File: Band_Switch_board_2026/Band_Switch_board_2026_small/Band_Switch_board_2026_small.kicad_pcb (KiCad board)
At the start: 2 copper layers, 90 x 40 mm, 29 parts, among them J1 KMDGX-8S-N, J2 AUX Out, J3 PTT Rig, J4 ICOM Band, J5 I2C Bus, J6 AUX Out, J7 PTT, J8 ADC Module, U1 ADS1015IDGS

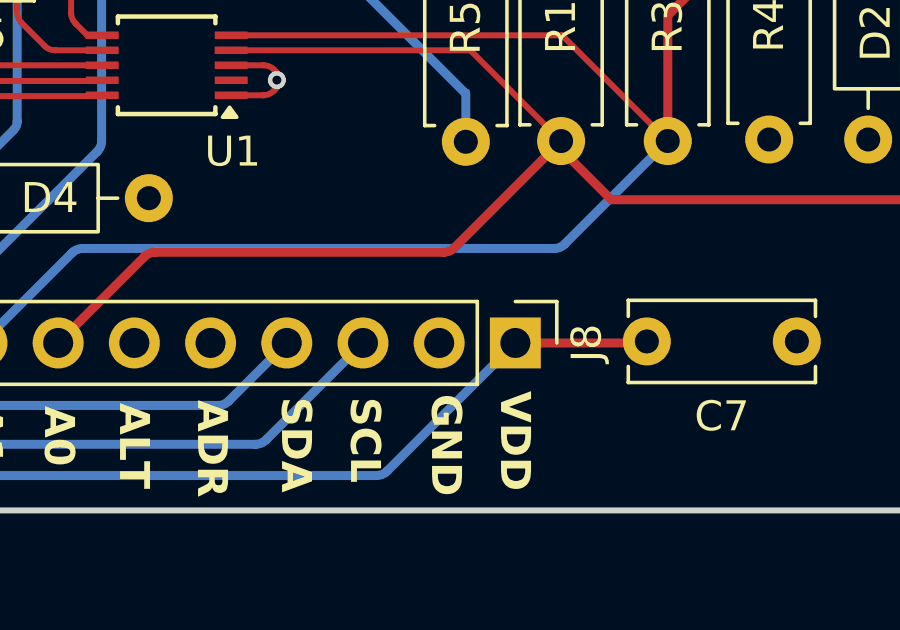
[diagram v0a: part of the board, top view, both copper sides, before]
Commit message: update pcb files to kicad 10
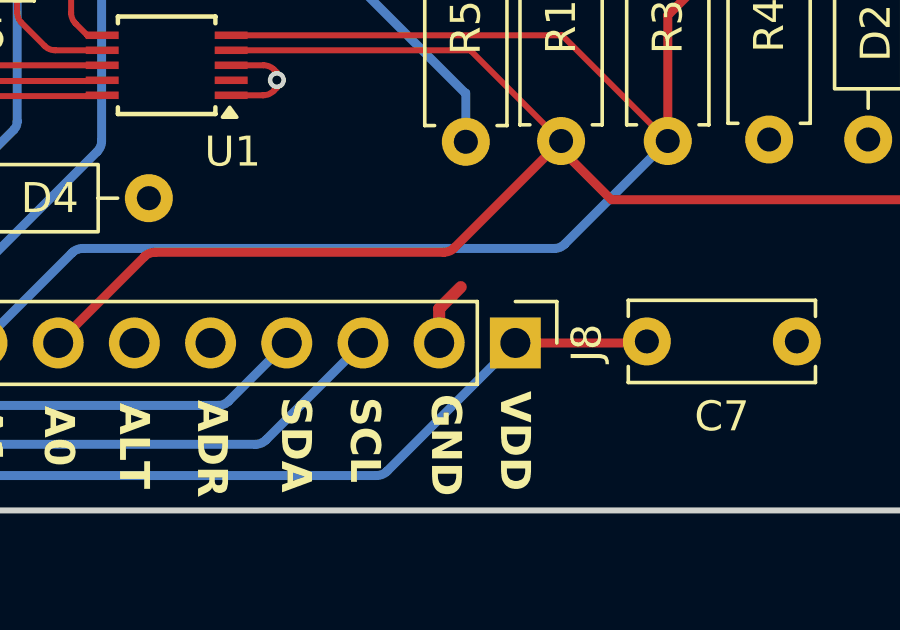
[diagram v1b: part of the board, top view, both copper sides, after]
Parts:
- J8: value ADC Module -> ADC Module Option
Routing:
- net GND: track 3.71 -> 5.87 mm

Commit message: change some values - alter boards
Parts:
- added C8: 100nf, Capacitor_THT:C_Disc_D6.0mm_W2.5mm_P5.00mm, F.Cu at (158.0, 84.2)
- added U2: 24LC32, Package_DIP:DIP-8_W7.62mm_Socket, F.Cu at (149.3, 76.7)
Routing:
- net /SCL: track 76.5 -> 101.6 mm
- net /SDA: track 72.9 -> 98.0 mm
- net +5V: track 109.3 -> 133.8 mm
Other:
- board size 90 x 40 mm -> 90 x 45 mm
- board text added: "EEPROM"
